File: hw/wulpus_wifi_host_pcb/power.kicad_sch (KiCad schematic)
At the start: 9 parts, among them J1 SM02B-PASS-TBT_LF__SN_, Q1 LP0404N3T5G, Q2 LP0404N3T5G, Q3 FS8205A, U1 TPS63900DSKR, U2 TPS63900DSKR, U3 BQ29700DSER

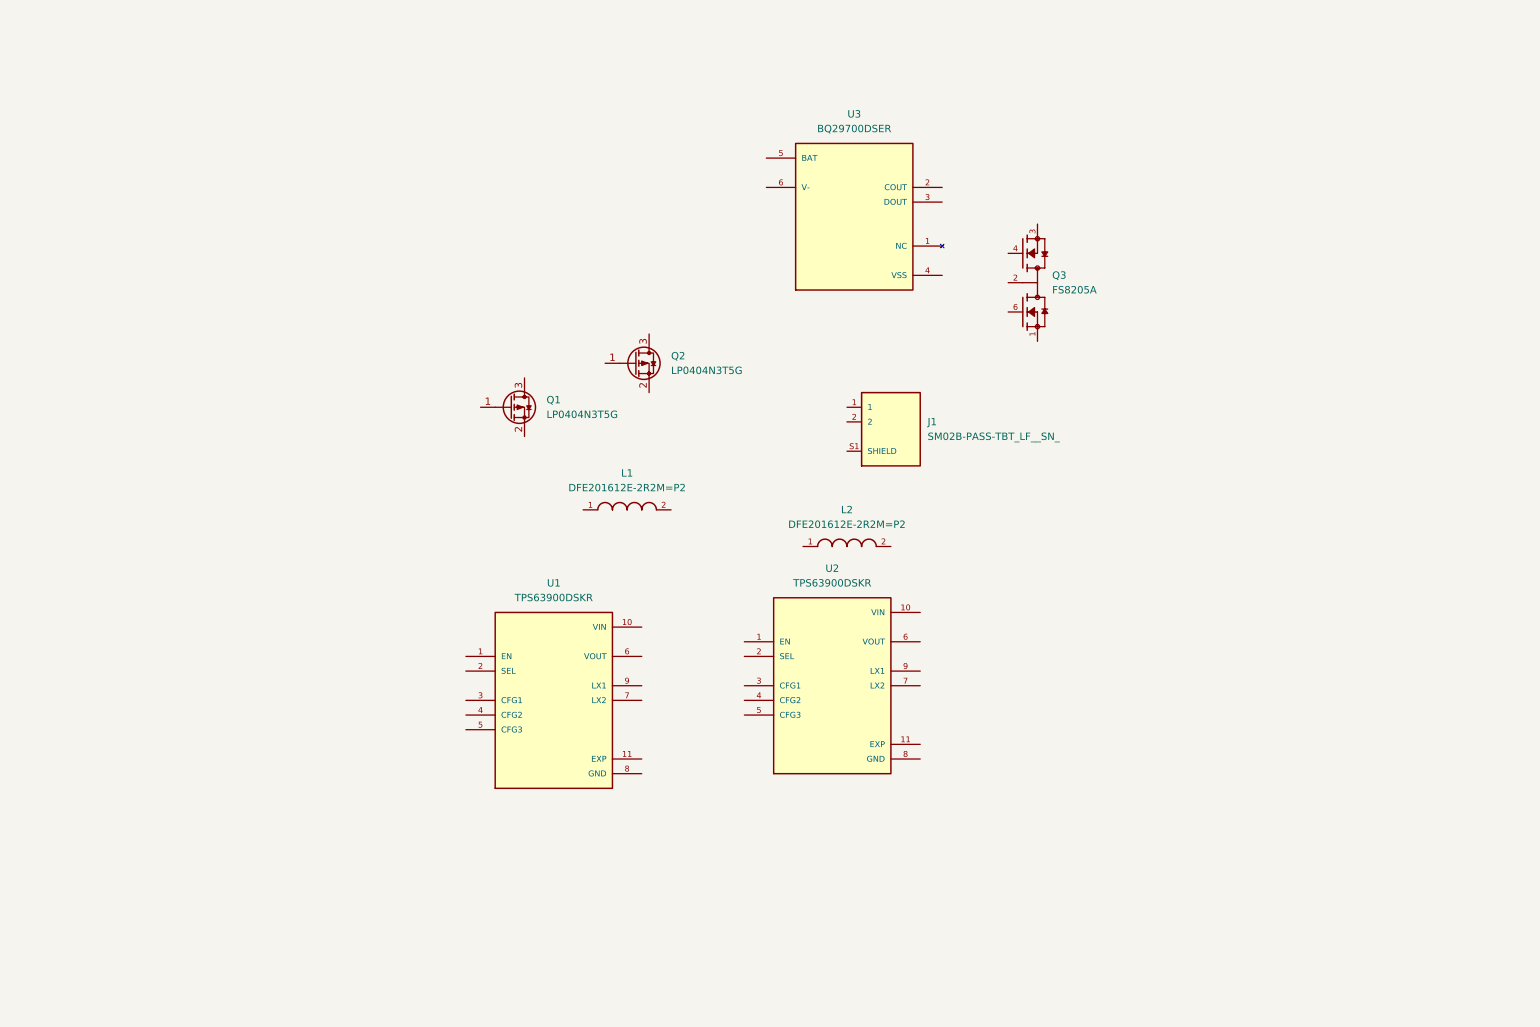
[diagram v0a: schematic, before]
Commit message: Added hierarchical shets, signals for esp32 and battery protector ref schematic
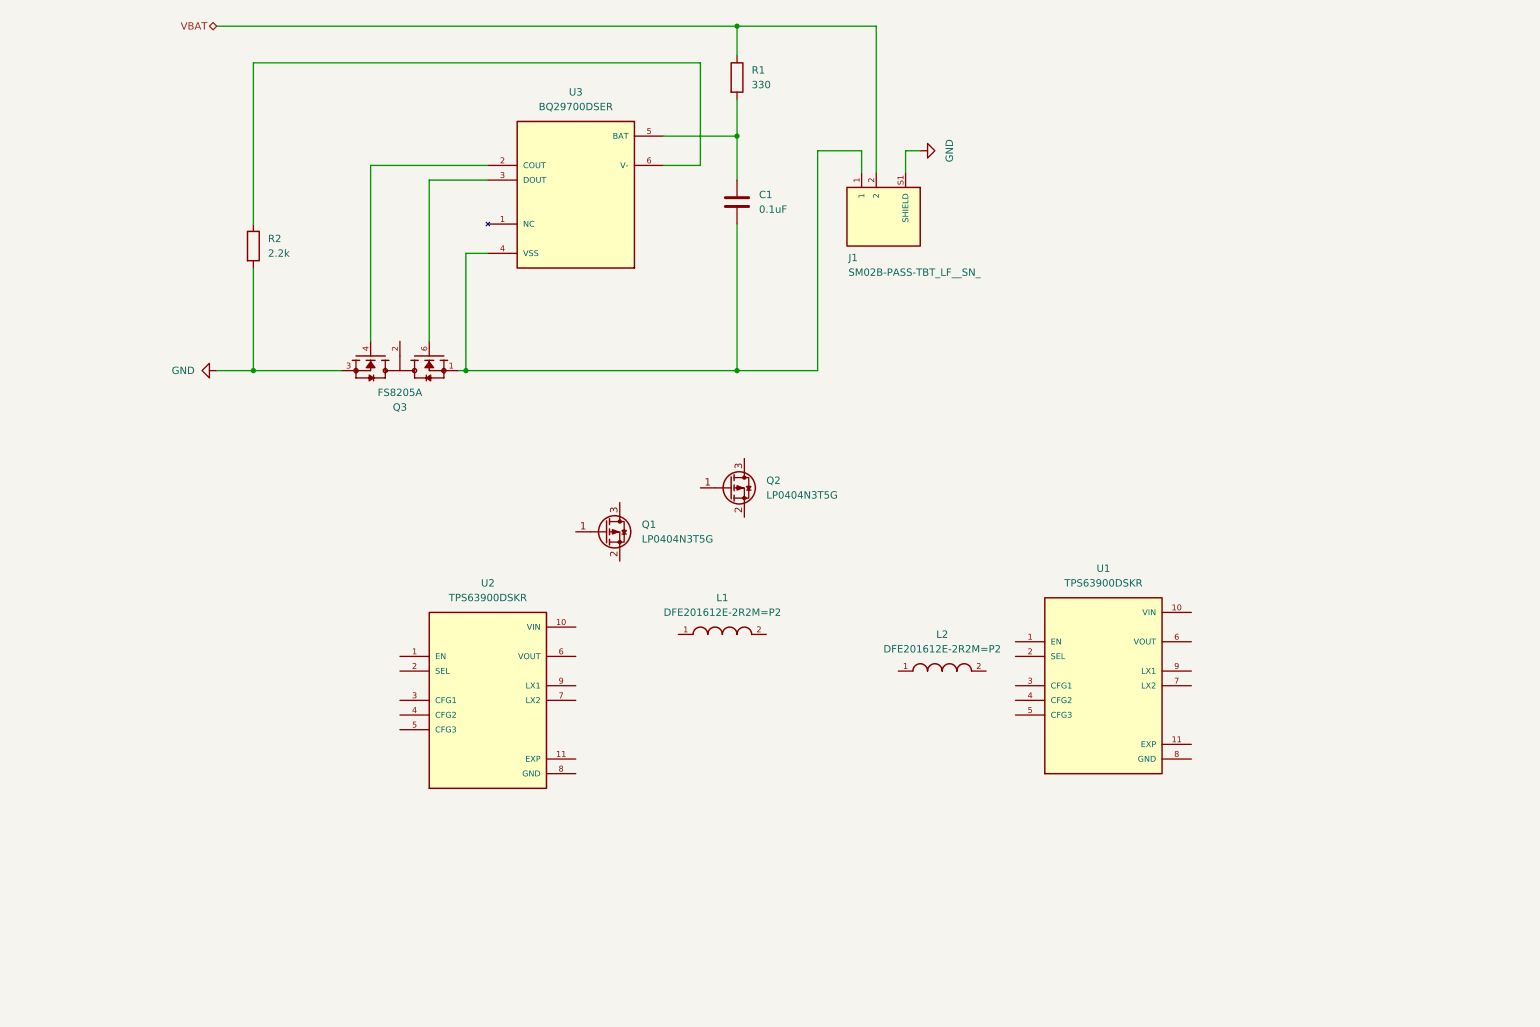
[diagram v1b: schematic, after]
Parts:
- added C1: 0.1uF, Capacitor_SMD:C_01005_0402Metric, symbol Device:C
- added R1: 330, Resistor_SMD:R_0402_1005Metric, symbol Device:R
- added R2: 2.2k, Resistor_SMD:R_0402_1005Metric, symbol Device:R
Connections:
- net at U3.2 (COUT): now also Q3.4
- net at U3.3 (DOUT): now also Q3.6
- net at U3.4 (VSS): now also J1.1, Q3.1, C1.2
- net at U3.5 (BAT): now also C1.1, R1.2
- net at U3.6 (V-): now also R2.1
- net VBAT: now reaches J1.2
- net VBAT: now also R1.1
- net GND: now reaches J1.S1 (SHIELD), J1.S2 (SHIELD)
- net GND: now also Q3.3, R2.2
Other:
- moved on the sheet: J1, L1, L2, Q1, Q2, Q3, U1, U2, U3

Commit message: Partially added DC-DCs
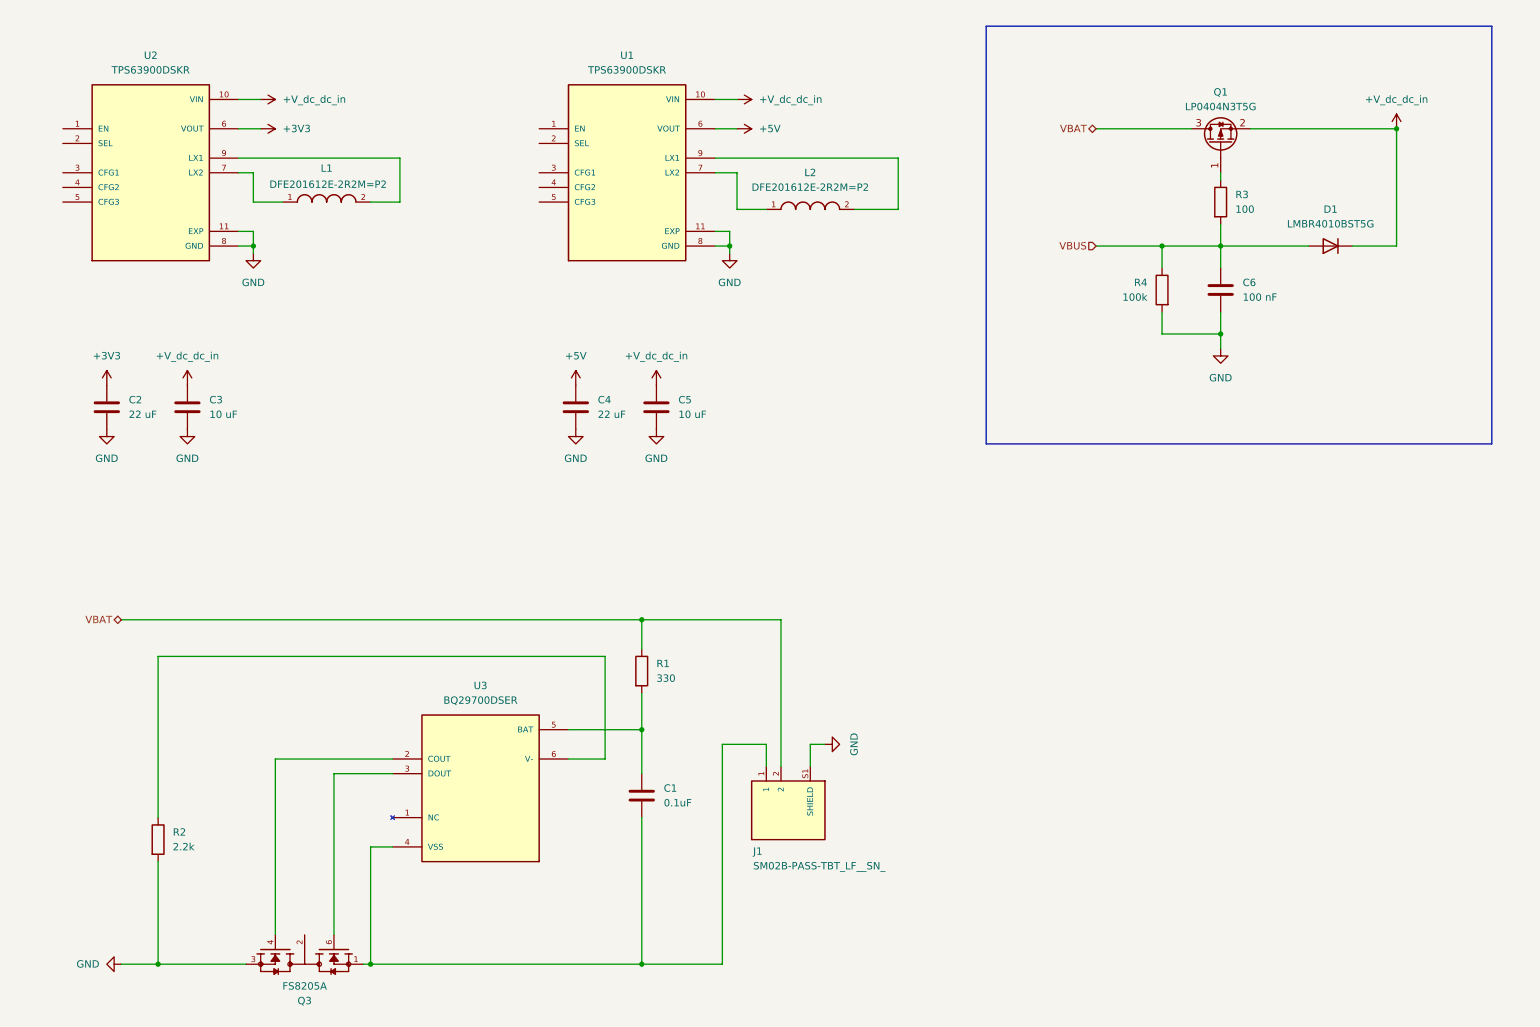
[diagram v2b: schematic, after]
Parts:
- removed Q2: LP0404N3T5G, Package_TO_SOT_SMD:SOT-883, symbol Transistor_FET:Q_PMOS_GSD
- added C2, C4: 22 uF, Capacitor_SMD:C_01005_0402Metric, symbol Device:C
- added C3, C5: 10 uF, Capacitor_SMD:C_01005_0402Metric, symbol Device:C
- added C6: 100 nF, Capacitor_SMD:C_01005_0402Metric, symbol Device:C
- added D1: LMBR4010BST5G, Diode_SMD:D_SOD-882, symbol Device:D
- added R3: 100, Resistor_SMD:R_0402_1005Metric, symbol Device:R
- added R4: 100k, Resistor_SMD:R_0402_1005Metric, symbol Device:R
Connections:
- net GND: now also U1.11 (EXP), U1.8 (GND), U2.11 (EXP), U2.8 (GND), C2.2, C3.2, C4.2, C5.2, C6.2, R4.2
- net VBAT: now also Q1.3 (D)
- net +V_dc_dc_in: now reaches U1.10 (VIN)
- net +V_dc_dc_in: now also Q1.2 (S), U2.10 (VIN), C3.1, C5.1, D1.1 (K)
- net +5V: now reaches U1.6 (VOUT)
- net +5V: now also C4.1
- net at U1.7 (LX2): now also L2.1
- net at U1.9 (LX1): now also L2.2
- net at Q1.1 (G): now also R3.1
- net at L1.1: now also U2.7 (LX2)
- net at L1.2: now also U2.9 (LX1)
- net +3V3: now reaches U2.6 (VOUT)
- net +3V3: now also C2.1
- new net VBUS: C6.1, D1.2 (A), R3.2, R4.1
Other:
- moved on the sheet: C1, J1, L1, L2, Q1, Q3, R1, R2, U1, U2, U3

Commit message: Updated footprints, mapped 3D models, added layerstack, partial placement and layout
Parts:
- removed J1: SM02B-PASS-TBT_LF__SN_, Ultrasound:JST_SM02B-PASS-TBT_LF__SN_, symbol Ultrasound:SM02B-PASS-TBT_LF__SN_
- added J1: S2B-PH-SM4-TB_LF__SN_, Ultrasound:JST_S2B-PH-SM4-TB_LF__SN_, symbol Ultrasound:S2B-PH-SM4-TB_LF__SN_
- added R12, R18: 0, Resistor_SMD:R_0402_1005Metric, symbol Device:R
- added R13, R20: o, Resistor_SMD:R_0402_1005Metric, symbol Device:R
- added R15: 16.2k, Resistor_SMD:R_0402_1005Metric, symbol Device:R
- added R16, R17: 5.1M, Resistor_SMD:R_0402_1005Metric, symbol Device:R
- added R21: 36.5k, Resistor_SMD:R_0402_1005Metric, symbol Device:R
- added TP1, TP2, TP3: TestPoint, TestPoint:TestPoint_Pad_1.0x1.0mm, symbol Connector:TestPoint
- added TP5: TestPoint, TestPoint:TestPoint_Pad_1.5x1.5mm, symbol Connector:TestPoint
- C1: renamed from C2; footprint Capacitor_SMD:C_01005_0402Metric -> Capacitor_SMD:C_0402_1005Metric
- C2: renamed from C3; footprint Capacitor_SMD:C_01005_0402Metric -> Capacitor_SMD:C_0402_1005Metric
- C3: renamed from C1; footprint Capacitor_SMD:C_01005_0402Metric -> Capacitor_SMD:C_0402_1005Metric
- C4, C5, C6: footprint Capacitor_SMD:C_01005_0402Metric -> Capacitor_SMD:C_0402_1005Metric
- Q1: renamed from Q3; MF Fortune Semiconductor -> Evvo/Fuxin semi
- renumbered Q1 to Q2, R2 to R14, R1 to R19, R4 to R22, R3 to R23, U1 to U4
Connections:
- net +V_dc_dc_in is gone; now on net +V_board: C2.1, C5.1, D1.1 (K), Q2.2 (S), U2.10 (VIN), U4.10 (VIN)
- net +3V3: now also TP1.1
- net +5V: now also TP2.1
- net GND: now also U2.2 (SEL), U4.2 (SEL), J1.S1 (SHIELD), J1.S2 (SHIELD), R12.2, R13.2, R15.1, R16.2, R18.2, R20.2, R21.1
- net VBAT: now also J1.1
- net +V_board: now reaches U4.1 (EN)
- net +V_board: now also U2.1 (EN), TP3.1
- net at U4.3 (CFG1): now also R18.1
- net at U4.4 (CFG2): now also R20.1
- net at U4.5 (CFG3): now also R21.2
- net at Q1.4, U3.2 (COUT): now also R16.1
- net at Q1.6, U3.3 (DOUT): now also R17.1
- net at C3.2, Q1.1, U3.4 (VSS): now also J1.2, R17.2
- net at Q1.2, Q1.5: now also TP5.1
- net at U2.3 (CFG1): now also R12.1
- net at U2.4 (CFG2): now also R13.1
- net at U2.5 (CFG3): now also R15.2
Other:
- note added: "+3v3 and +5V0 DC-DC converters"
- note added: "Battery Protection"
- note added: "CELL+"
- note added: "CELL-"
- note added: "PACK+"
- note added: "PACK-"
- note added: "USB/Battery Power OR Switch"
- moved on the sheet: C1, C2, C3, C4, C5, C6, D1, L1, L2, Q1, Q2, R14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

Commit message: Added preliminary layout
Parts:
- TP5: footprint TestPoint:TestPoint_Pad_1.5x1.5mm -> TestPoint:TestPoint_Pad_1.0x1.0mm
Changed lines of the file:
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@@
 			)
 		)
-		(property "Footprint" "TestPoint:TestPoint_Pad_1.5x1.5mm"
+		(property "Footprint" "TestPoint:TestPoint_Pad_1.0x1.0mm"
 			(at 58.42 177.8 0)
 			(hide yes)

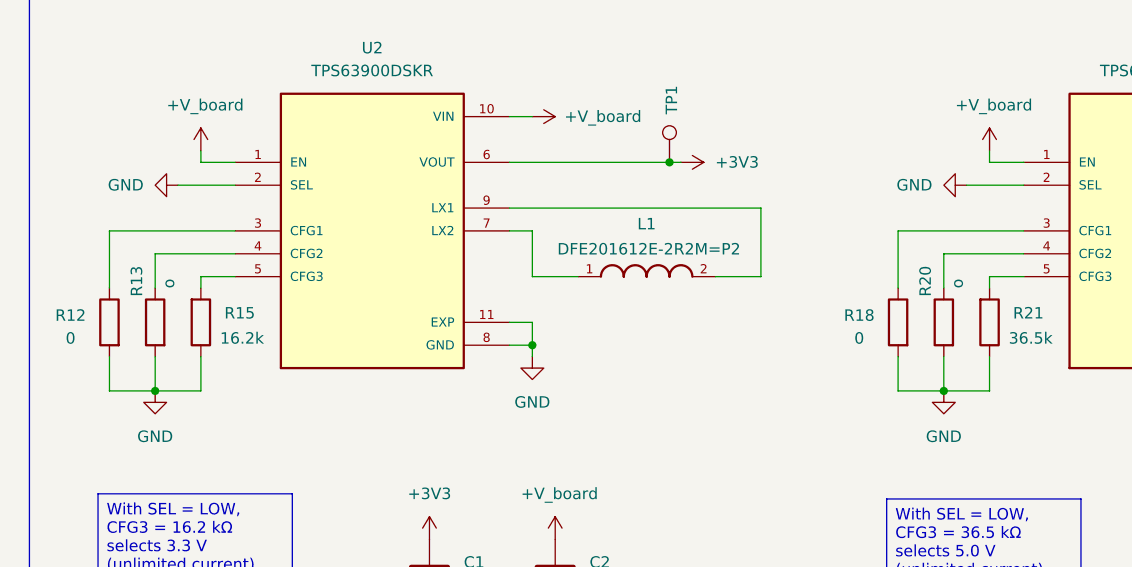
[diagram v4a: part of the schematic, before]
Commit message: Changed cap footprints to 0603
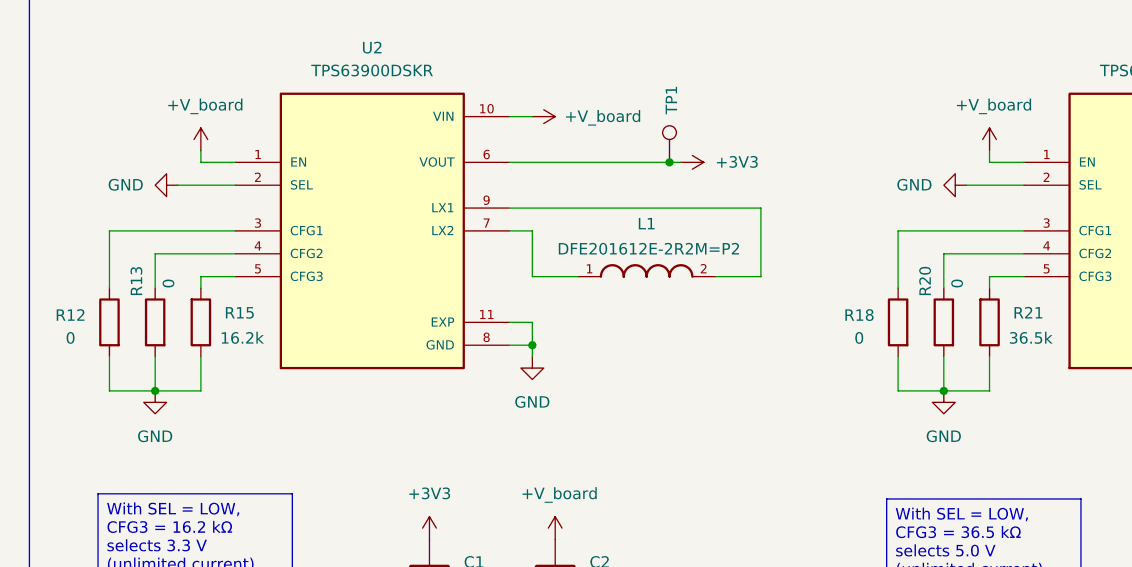
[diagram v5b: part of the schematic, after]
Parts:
- C1, C2, C4, C5: footprint Capacitor_SMD:C_0402_1005Metric -> Capacitor_SMD:C_0603_1608Metric
- D1: MANUFACTURER (none) -> LRC; MP (none) -> LMBR4010BST5G
- L1, L2: MANUFACTURER (none) -> Murata Electronics
- Q1: MANUFACTURER Fortune -> FUXINSEMI; MP FS8205 -> FS8205A
- Q2: MANUFACTURER (none) -> LRC; MP (none) -> LP0404N3T5G
- R13, R20: value o -> 0
- TP1, TP2, TP3, TP5: now left out of the parts list
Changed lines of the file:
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@@
 			)
 		)
-		(property "Footprint" "Capacitor_SMD:C_0402_1005Metric"
+		(property "Footprint" "Capacitor_SMD:C_0603_1608Metric"
 			(at 63.1952 93.98 0)
 			(hide yes)
@@
 		(body_style 1)
 		(exclude_from_sim no)
-		(in_bom yes)
+		(in_bom no)
 		(on_board yes)
 		(in_pos_files yes)
@@
 			)
 		)
-		(property "Footprint" "Capacitor_SMD:C_0402_1005Metric"
+		(property "Footprint" "Capacitor_SMD:C_0603_1608Metric"
 			(at 77.1652 93.98 0)
 			(hide yes)
@@
 			)
 		)
+		(property "MP" "LP0404N3T5G"
+			(at 237.49 55.88 90)
+			(hide yes)
+			(show_name no)
+			(do_not_autoplace no)
+			(effects
+				(font
+					(size 1.27 1.27)
+				)
+			)
+		)
+		(property "MANUFACTURER" "LRC"
+			(at 237.49 55.88 90)
+			(hide yes)
+			(show_name no)
+			(do_not_autoplace no)
+			(effects
+				(font
+					(size 1.27 1.27)
+				)
+			)
+		)
 		(pin "1"
 		)
@@
 			)
 		)
-		(property "Value" "o"
+		(property "Value" "0"
 			(at 33.274 57.912 90)
 			(show_name no)
@@
 			)
 		)
+		(property "MANUFACTURER" "Murata Electronics"
+			(at 175.26 58.42 0)
+			(hide yes)
+			(show_name no)
+			(do_not_autoplace no)
+			(effects
+				(font
+					(size 1.27 1.27)
+				)
+			)
+		)
 		(pin "1"
 		)
@@
 			)
 		)
+		(property "MANUFACTURER" "Murata Electronics"
+			(at 86.36 57.15 0)
+			(hide yes)
+			(show_name no)
+			(do_not_autoplace no)
+			(effects
+				(font
+					(size 1.27 1.27)
+				)
+			)
+		)
 		(pin "2"
 		)
@@
 			)
 		)
+		(property "MP" "LMBR4010BST5G"
+			(at 256.54 73.66 0)
+			(hide yes)
+			(show_name no)
+			(do_not_autoplace no)
+			(effects
+				(font
+					(size 1.27 1.27)
+				)
+			)
+		)
+		(property "MANUFACTURER" "LRC"
+			(at 256.54 73.66 0)
+			(hide yes)
+			(show_name no)
+			(do_not_autoplace no)
+			(effects
+				(font
+					(size 1.27 1.27)
+				)
+			)
+		)
 		(pin "1"
 		)
@@
 			)
 		)
-		(property "Footprint" "Capacitor_SMD:C_0402_1005Metric"
+		(property "Footprint" "Capacitor_SMD:C_0603_1608Metric"
 			(at 152.0952 93.98 0)
 			(hide yes)
@@
 			)
 		)
-		(property "MP" "FS8205"
+		(property "MP" "FS8205A"
 			(at 53.34 182.88 0)
 			(hide yes)
@@
 			)
 		)
-		(property "MANUFACTURER" "Fortune"
+		(property "MANUFACTURER" "FUXINSEMI"
 			(at 53.34 182.88 0)
 			(hide yes)
@@
 		(body_style 1)
 		(exclude_from_sim no)
-		(in_bom yes)
+		(in_bom no)
 		(on_board yes)
 		(in_pos_files yes)
@@
 		(body_style 1)
 		(exclude_from_sim no)
-		(in_bom yes)
+		(in_bom no)
 		(on_board yes)
 		(in_pos_files yes)
@@
 			)
 		)
-		(property "Value" "o"
+		(property "Value" "0"
 			(at 120.904 57.912 90)
 			(show_name no)
@@
 		(body_style 1)
 		(exclude_from_sim no)
-		(in_bom yes)
+		(in_bom no)
 		(on_board yes)
 		(in_pos_files yes)
@@
 			)
 		)
-		(property "Footprint" "Capacitor_SMD:C_0402_1005Metric"
+		(property "Footprint" "Capacitor_SMD:C_0603_1608Metric"
 			(at 166.0652 93.98 0)
 			(hide yes)

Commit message: Fixed BOM, added jobset file, regenerated fabrication outputs
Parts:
- C1, C4: MANUFACTURER (none) -> Murata Electronics; MP (none) -> GRM187R60J226ME15
- C2, C5: MANUFACTURER (none) -> Murata Electronics; MP (none) -> GRM188R61A106ME69
- C3: value 0.1uF -> 100 nF; MANUFACTURER (none) -> Murata Electronics; MP (none) -> GCM155R71H104KE02J
- C6: MANUFACTURER (none) -> Murata Electronics; MP (none) -> GCM155R71H104KE02J
- R12, R13, R18, R20: MANUFACTURER (none) -> Yageo; MP (none) -> RC0402JR-070RL
- R14: MANUFACTURER (none) -> Yageo; MP (none) -> RC0402FR-072K2L
- R15: MANUFACTURER (none) -> Yageo; MP (none) -> RC0402FR-0716K2L
- R16, R17: MANUFACTURER (none) -> Yageo; MP (none) -> RC0402FR-075M1L
- R19: MANUFACTURER (none) -> Yageo; MP (none) -> RC0402FR-07330RL
- R21: MANUFACTURER (none) -> Yageo; MP (none) -> RC0402FR-0736K5L
- R22: MANUFACTURER (none) -> Yageo; MP (none) -> RC0402FR-07100KL
- R23: MANUFACTURER (none) -> Yageo; MP (none) -> RC0402FR-07100RL

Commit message: Added out capacitors for DC-DCs, regenerated fabrication files
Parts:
- added C1, C5: 22 uF, Capacitor_SMD:C_0603_1608Metric, symbol Device:C
- renumbered C1 to C2, C2 to C3, C3 to C4, C4 to C6, C5 to C7, C6 to C8, TP5 to TP1, TP1 to TP2, TP2 to TP3, TP3 to TP4
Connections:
- net +3V3: now also C1.1
- net +5V: now also C5.1
- net GND: now also C1.2, C5.2
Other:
- moved on the sheet: C2, C3, C6, C7

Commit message: Rename project to WULPUS Pro Max
- update user-facing branding across documentation, firmware, and software
- update repository URLs while preserving compatibility identifiers
- release WiFi host PCB v1.0.1 with revised metadata and silkscreen
- regenerate hardware design and fabrication outputs
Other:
- title: (none) -> WULPUS Pro Max WiFi host
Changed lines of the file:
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@@
 	(generator_version "10.0")
 	(paper "A4")
+	(title_block
+		(title "WULPUS Pro Max WiFi host")
+		(rev "v1.0.1")
+		(comment 1 "Reviewer: Cedric Hirschi")
+		(comment 2 "Author: Sergei Vostrikov")
+	)
 	(rectangle
 		(start 17.78 19.05)
